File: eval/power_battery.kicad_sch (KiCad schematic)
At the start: 4 parts, among them U18 HYG015N03LS1C2, U19 HYG015N03LS1C2, U7 MX74502D23_C41433189

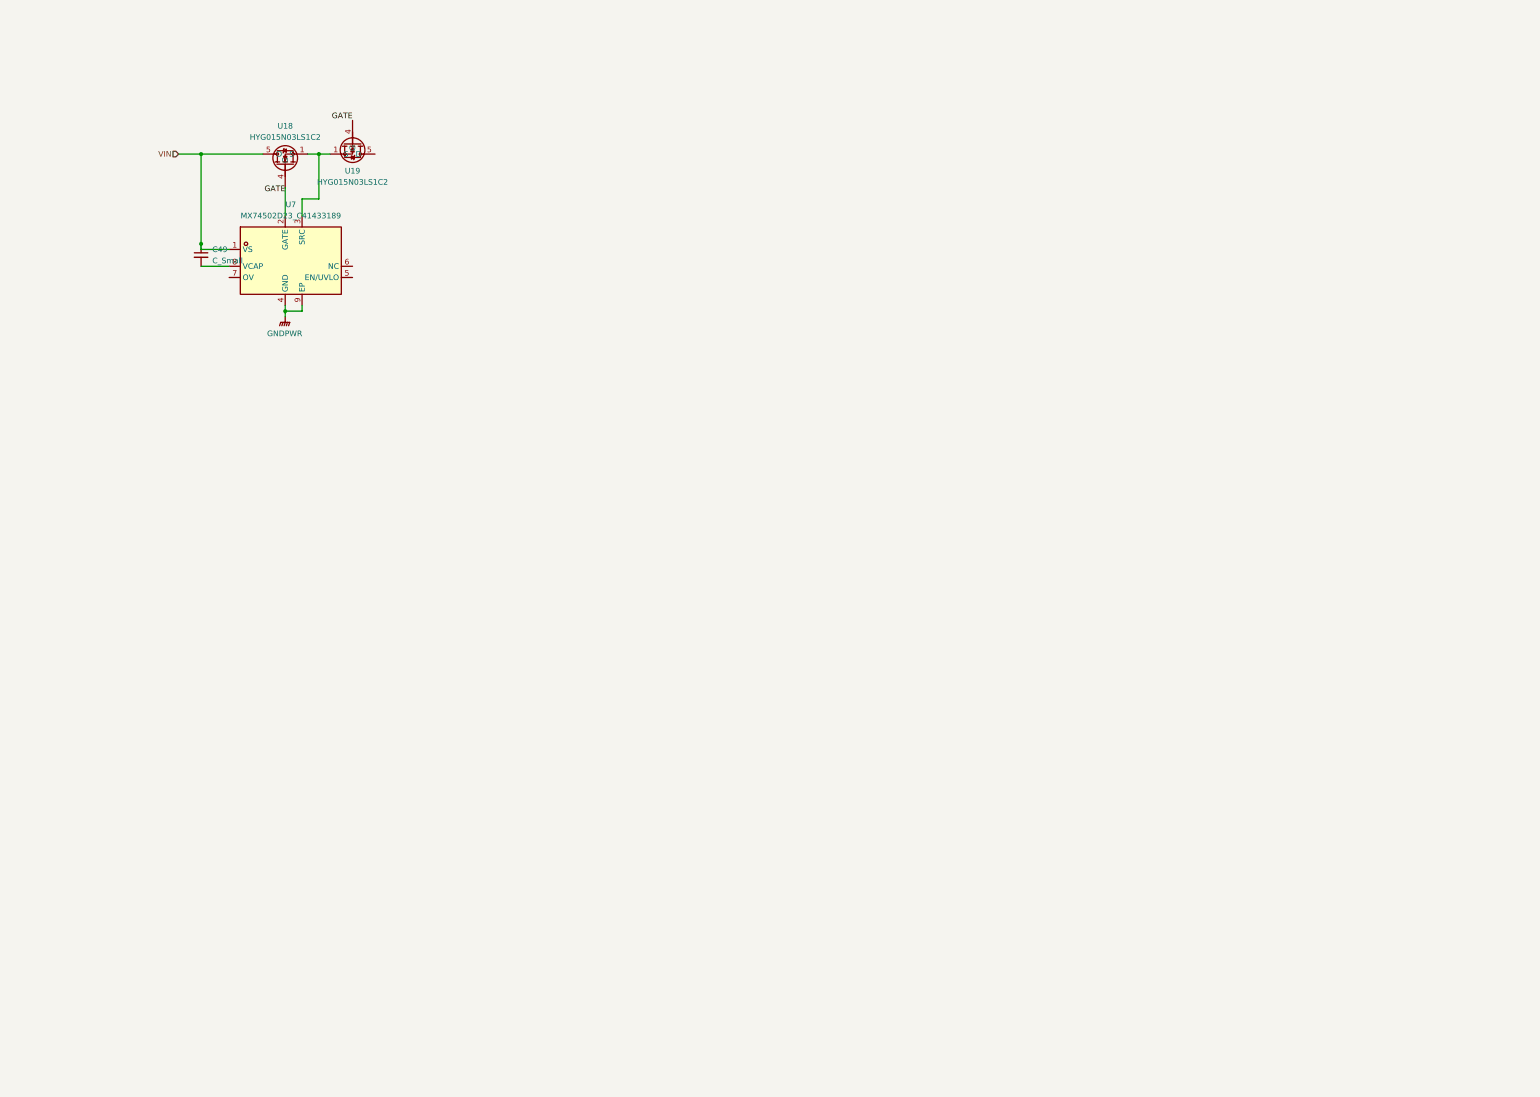
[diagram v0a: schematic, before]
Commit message: [sch]power_battery: add feature voltage drop, current rush, MCU input, reverse protection
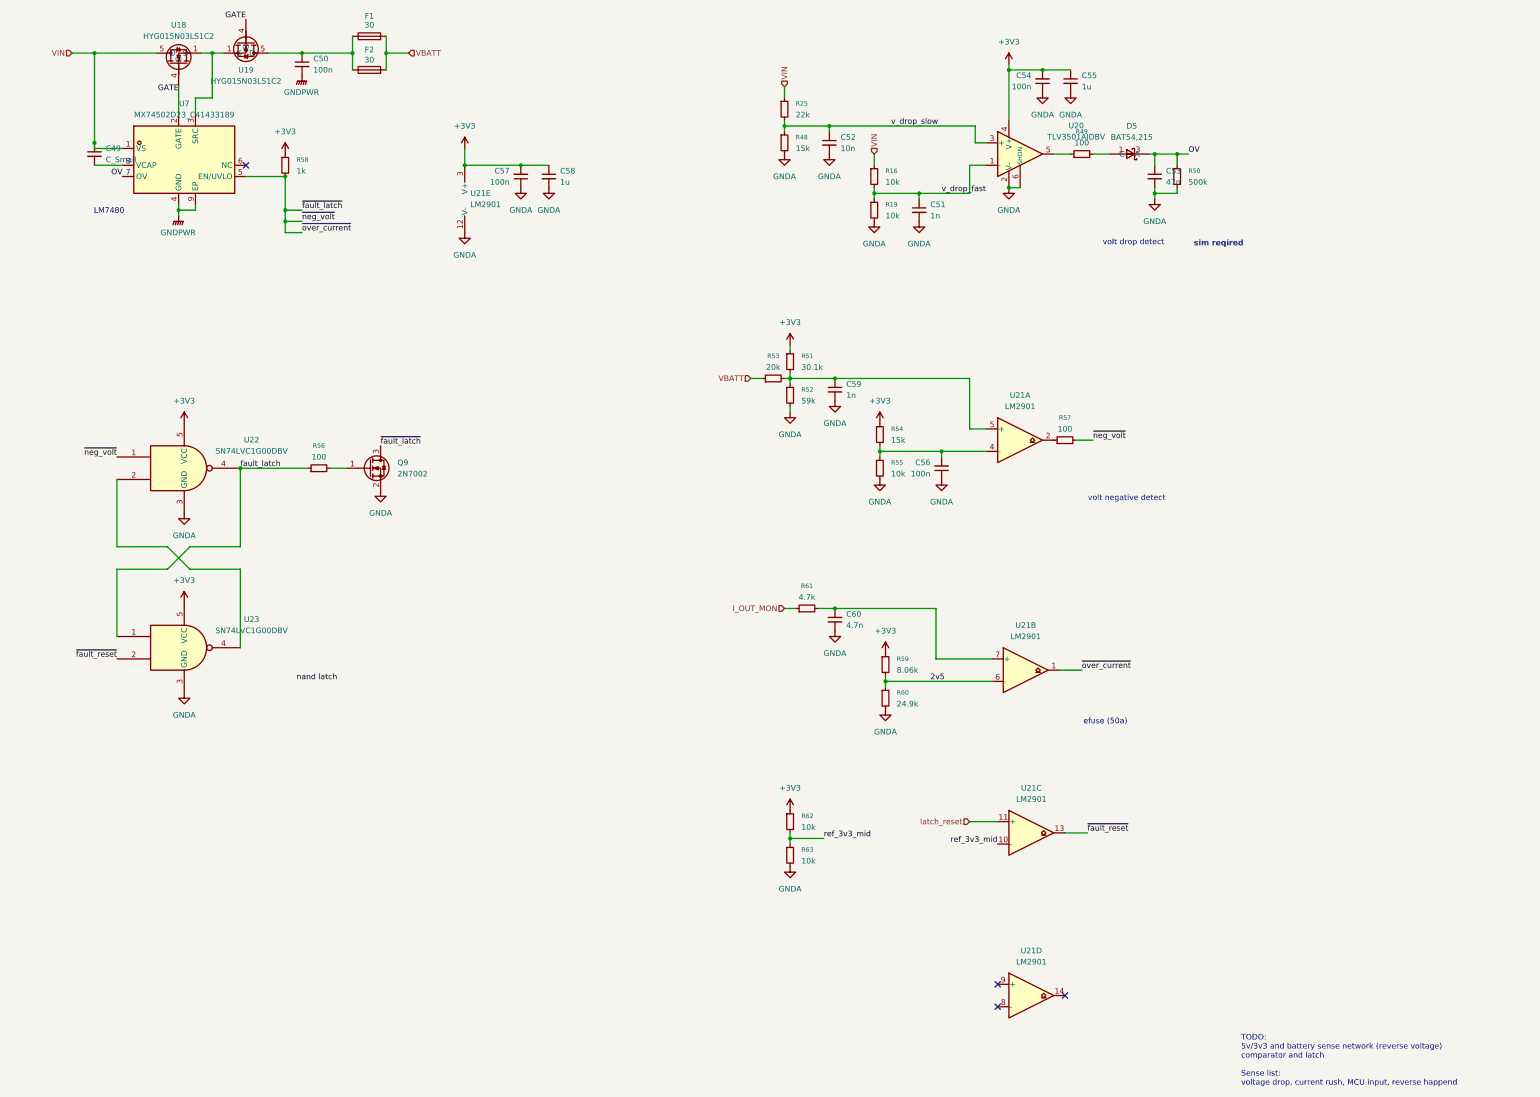
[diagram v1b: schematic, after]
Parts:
- added C50, C54, C56, C57: 100n, symbol Device:C_Small
- added C51, C59: 1n, symbol Device:C_Small
- added C52: 10n, symbol Device:C_Small
- added C53: 47n, symbol Device:C_Small
- added C55, C58: 1u, symbol Device:C_Small
- added C60: 4.7n, symbol Device:C_Small
- added D5: BAT54,215, EasyEDA:SOT-23_L2.9-W1.3-P1.90-LS2.4-BR, symbol EasyEDA:BAT54,215
- added F1, F2: 30, symbol Device:Fuse
- added Q9: 2N7002, Package_TO_SOT_SMD:SOT-23, symbol Transistor_FET:2N7002
- added R16, R19, R55, R62, R63: 10k, symbol Device:R_Small
- added R25: 22k, symbol Device:R_Small
- added R48, R54: 15k, symbol Device:R_Small
- added R49, R56, R57: 100, symbol Device:R_Small
- added R50: 500k, symbol Device:R_Small
- added R51: 30.1k, symbol Device:R_Small
- added R52: 59k, symbol Device:R_Small
- added R53: 20k, symbol Device:R_Small
- added R58: 1k, symbol Device:R_Small
- added R59: 8.06k, symbol Device:R_Small
- added R60: 24.9k, symbol Device:R_Small
- added R61: 4.7k, symbol Device:R_Small
- added U20: TLV3501AIDBV, Package_SO:SOIC-8_3.9x4.9mm_P1.27mm, symbol Comparator:TLV3501AIDBV
- added U21: LM2901, Package_SO:TSSOP-14_4.4x5mm_P0.65mm, symbol Comparator:LM2901
- added U22, U23: SN74LVC1G00DBV, Package_TO_SOT_SMD:SOT-23-5, symbol 74xGxx:SN74LVC1G00DBV
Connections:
- net GNDPWR: now also C50.2
- net VIN: now also R16.1, R25.1
- net ~{fault_latch}: now reaches U7.5 (EN/UVLO)
- net ~{fault_latch}: now also Q9.3 (D), R57.2, R58.2, U21.1, U22.1
- net OV: now reaches U7.7 (OV)
- net OV: now also C53.1, D5.3 (C), R50.1
- net at U19.5 (D), U19.6 (D), U19.7 (D)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: now also C50.1, F1.1, F2.1
- new net: C56.2, R54.2, R55.1, U21.4 (-)
- new net: U22.2, U23.4
- new net: C60.1, R61.2, U21.7 (+)
- new net: C59.1, R51.2, R52.1, R53.2, U21.5 (+)
- new net: R57.1, U21.2
- new net: R49.1, U20.5
- new net: D5.1 (A), R49.2
- new net: Q9.1 (G), R56.2
- new net +3V3: C54.2, C55.1, C57.2, C58.1, R51.1, R54.1, R58.1, R59.1, R62.1, U20.4 (V+), U21.3 (V+), U22.5 (VCC), U23.5 (VCC)
- new net 2v5: R59.2, R60.1, U21.6 (-)
- new net GNDA: C51.2, C52.2, C53.2, C54.1, C55.2, C56.1, C57.1, C58.2, C59.2, C60.2, Q9.2 (S), R19.2, R48.2, R50.2, R52.2, R55.2, R60.2, R63.2, U20.2 (V-), U20.6 (SHDN), U21.12 (V-), U22.3 (GND), U23.3 (GND)
- new net I_OUT_MON: R61.1
- new net VBATT: F1.2, F2.2, R53.1
- new net fault_latch: R56.1, U22.4, U23.1
- new net latch_reset: U21.11 (+)
- new net ref_3v3_mid: R62.2, R63.1, U21.10 (-)
- new net v_drop_fast: C51.1, R16.2, R19.1, U20.1 (-)
- new net v_drop_slow: C52.1, R25.2, R48.1, U20.3 (+)
- new net ~{fault_reset}: U21.13, U23.2
- no-connect marks 0 -> 4
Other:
- note added: "LM7480"
- note added: "TODO: 5v/3v3 and battery sense network (reverse voltage) comparator and latch Sense list: voltage drop, current rush, MCU input, reverse happend"
- note added: "efuse (50a)"
- note added: "sim reqired"
- note added: "volt drop detect"
- note added: "volt negative detect"
- moved on the sheet: C49, U18, U19, U7

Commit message: [layout] first draft layout
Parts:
- removed R57: 100, symbol Device:R_Small
- removed R62, R63: 10k, symbol Device:R_Small
- removed U18, U19: HYG015N03LS1C2, EasyEDA:PDFN-8_L5.9-W5.2-P1.27-LS6.2-BL, symbol EasyEDA:HYG015N03LS1C2
- added C61: 1u, Capacitor_SMD:C_0603_1608Metric, symbol Device:C_Small
- added Q10: 2N7002, Package_TO_SOT_SMD:SOT-23, symbol Transistor_FET:2N7002
- added R64: 100k, Resistor_SMD:R_0603_1608Metric, symbol Device:R_Small
- added R65, R66: 1k, Resistor_SMD:R_0603_1608Metric, symbol Device:R_Small
- added TP1: neg_volt, symbol Connector:TestPoint
- added TP2: over_current, symbol Connector:TestPoint
- added TP4: drop_volt, symbol Connector:TestPoint
- added TP5: fault_latch, symbol Connector:TestPoint
- added TP6: power_on_hold_rc, symbol Connector:TestPoint
- added TP7: 74502_en, symbol Connector:TestPoint
- added TP8: 74502_ov, symbol Connector:TestPoint
- added TP9: fault_reset_mcu, symbol Connector:TestPoint
- added U24, U25: HYG015N03LS1C2, EasyEDA:PDFN-8_L5.9-W5.2-P1.27-LS6.2-BL, symbol EasyEDA:HYG015N03LS1C2
- C50, C51, C52, C53, C54, C55, C56, C57, C58, C59, C60: footprint (none) -> Capacitor_SMD:C_0603_1608Metric
- R16, R19, R25, R48, R49, R50, R51, R52, R53, R54, R55, R56, R58, R59, R60, R61: footprint (none) -> Resistor_SMD:R_0603_1608Metric
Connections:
- net latch_reset is gone; now on net i_mon_filter: U21.11 (+)
- net ref_3v3_mid is gone; now on net 2v5: U21.10 (-)
- net +3V3: now also C61.1, R65.1, R66.1
- net 2v5: no longer U21.6 (-)
- net GATE: now also U24.4 (G), U25.4 (G)
- net GNDA: now also Q10.2 (S), R64.2
- net OV: now also TP8.1
- net VBATT: no longer F1.2, F2.2
- net VIN: no longer C49.1, U7.1 (VS)
- net fault_latch: now also TP5.1
- net at C50.1, F1.1, F2.1: now also U25.5 (D), U25.6 (D), U25.7 (D), U25.8 (D), U25.9 (D)
- net vbat_comp_thre: now reaches C56.2, R54.2, R55.1, U21.4 (-)
- net i_mon_filter: now reaches C60.1, R61.2
- net i_mon_filter: no longer U21.7 (+)
- net vbat_none_neg: now reaches C59.1, R51.2, R52.1, R53.2, U21.5 (+)
- net power_on_hold: now reaches U21.2
- net power_on_hold: now also Q9.3 (D), R58.2, U21.13, U22.1, U7.5 (EN/UVLO), Q10.3 (D), R65.2, TP1.1, TP2.1, TP7.1
- net at R49.1, U20.5: now also TP4.1
- net at U7.3 (SRC): now also U24.1 (S), U24.2 (S), U24.3 (S), U25.1 (S), U25.2 (S), U25.3 (S)
- removed net ~{fault_latch}: Q9.3 (D), R58.2, U21.1, U22.1, U7.5 (EN/UVLO)
- net ~{fault_reset} renamed ~{fault_reset_mcu}
- net ~{fault_reset_mcu}: now also R66.2, TP9.1; no longer U21.13
- new net: C61.2, Q10.1 (G), R64.1, TP6.1
- new net FROM_BUCK: C49.1, U24.5 (D), U24.6 (D), U24.7 (D), U24.8 (D), U24.9 (D), U7.1 (VS)
- new net TO_BATT: F1.2, F2.2
- no-connect marks 4 -> 7
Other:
- moved on the sheet: Q9, R56, U22, U23

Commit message: [layout] 50*100mm, without trace
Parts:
- removed D5: BAT54,215, EasyEDA:SOT-23_L2.9-W1.3-P1.90-LS2.4-BR, symbol EasyEDA:BAT54,215
- removed U20: TLV3501AIDBV, Package_SO:SOIC-8_3.9x4.9mm_P1.27mm, symbol Comparator:TLV3501AIDBV
- removed U21: LM2901, Package_SO:TSSOP-14_4.4x5mm_P0.65mm, symbol Comparator:LM2901
- added D5: BAT54J, Diode_SMD:D_SOD-323F, symbol Diode:BAT54J
- added U18: TLV3501AIDBV, Package_TO_SOT_SMD:SOT-23-6, symbol Comparator:TLV3501AIDBV
- added U20: LM2903, Package_SO:TSSOP-8_4.4x3mm_P0.65mm, symbol Comparator:LM2903
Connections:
- net +3V3: now also U18.4 (V+), U20.8 (V+)
- net 2v5: now also U20.6 (-)
- net GNDA: now also U18.2 (V-), U18.6 (SHDN), U20.4 (V-)
- net OV: now also D5.1 (K)
- net i_mon_filter: now also U20.5 (+)
- net power_on_hold: now also U20.1, U20.7
- net v_drop_fast: now also U18.1 (-)
- net v_drop_slow: now also U18.3 (+)
- net vbat_comp_thre: now also U20.2 (-)
- net vbat_none_neg: now also U20.3 (+)
- net at R49.1, TP4.1: now also U18.5
- net at R49.2: now also D5.2 (A)
- no-connect marks 7 -> 1
